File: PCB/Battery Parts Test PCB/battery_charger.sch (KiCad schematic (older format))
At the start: 43 parts, among them P5 CONN_2, P6 CONN_2, P7 CONN_2, P8 CONN_2, P9 CONN_2, Q13 MOSFET_N, Q14 MOSFET_P, Q15 MOSFET_P, T1 TRANSFO, U3 LTC4000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

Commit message: updated schematic
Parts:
- added C32: C, symbol C
- added R60: R, symbol R
- C31: value C -> 0.1uF
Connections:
- net CONV_OUT: now also C30.1
- net at P8.1 (P1), Q15.S, R50.2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: now also C31.1
- net at U3.24 (ITH), U4.2 (ITH): now also R60.2
- net at U3.25 (CC): now also C32.1
- new net: C32.2, R60.1
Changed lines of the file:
@@
-EESchema Schematic File Version 2  date 4/30/2013 1:48:29 PM
+EESchema Schematic File Version 2  date 5/7/2013 3:13:49 PM
 LIBS:power
 LIBS:device
@@
 Sheet 9 9
 Title ""
-Date "30 apr 2013"
+Date "7 may 2013"
 Rev ""
 Comp ""
@@
 Comment4 ""
 $EndDescr
-Text Label 8900 2150 0    60   ~ 0
-BATT+
+Connection ~ 9700 1350
+Wire Wire Line
+	9700 1350 10500 1350
+Wire Wire Line
+	5250 3800 5050 3800
+Wire Wire Line
+	5050 3800 5050 2650
+Wire Wire Line
+	5050 2650 5200 2650
 Connection ~ 8250 4300
 Wire Wire Line
@@
 Wire Wire Line
 	6850 4300 7350 4300
+Connection ~ 8850 5800
+Wire Wire Line
+	6150 3800 6150 3600
+Connection ~ 6150 3600
+$Comp
+L R R60
+U 1 1 518484F7
+P 5900 3800
+F 0 "R60" V 5980 3800 50  0000 C CNN
+F 1 "R" V 5900 3800 50  0000 C CNN
+	1    5900 3800
+	0    -1   -1   0
+$EndComp
+$Comp
+L C C32
+U 1 1 518484F3
+P 5450 3800
+F 0 "C32" H 5500 3900 50  0000 L CNN
+F 1 "C" H 5500 3700 50  0000 L CNN
+	1    5450 3800
+	0    -1   -1   0
+$EndComp
+Text Label 8900 2150 0    60   ~ 0
+BATT+
 Text Label 6350 850  0    60   ~ 0
 VIN
@@
 CONV_OUT
 $Comp
-L GND #PWR9
+L GND #PWR011
 U 1 1 51756554
 P 6350 4950
-F 0 "#PWR9" H 6350 4950 30  0001 C CNN
+F 0 "#PWR011" H 6350 4950 30  0001 C CNN
 F 1 "GND" H 6350 4880 30  0001 C CNN
 	1    6350 4950
@@
 $EndComp
 $Comp
-L GND #PWR11
+L GND #PWR012
 U 1 1 517562CD
 P 6500 6400
-F 0 "#PWR11" H 6500 6400 30  0001 C CNN
+F 0 "#PWR012" H 6500 6400 30  0001 C CNN
 F 1 "GND" H 6500 6330 30  0001 C CNN
 	1    6500 6400
@@
 $EndComp
 $Comp
-L GND #PWR16
+L GND #PWR013
 U 1 1 5175625C
 P 8600 6400
-F 0 "#PWR16" H 8600 6400 30  0001 C CNN
+F 0 "#PWR013" H 8600 6400 30  0001 C CNN
 F 1 "GND" H 8600 6330 30  0001 C CNN
 	1    8600 6400
@@
 $EndComp
 $Comp
-L GND #PWR12
+L GND #PWR014
 U 1 1 517560C1
 P 6650 5100
-F 0 "#PWR12" H 6650 5100 30  0001 C CNN
+F 0 "#PWR014" H 6650 5100 30  0001 C CNN
 F 1 "GND" H 6650 5030 30  0001 C CNN
 	1    6650 5100
@@
 $EndComp
 $Comp
-L GND #PWR18
+L GND #PWR015
 U 1 1 51755E2F
 P 10150 2350
-F 0 "#PWR18" H 10150 2350 30  0001 C CNN
+F 0 "#PWR015" H 10150 2350 30  0001 C CNN
 F 1 "GND" H 10150 2280 30  0001 C CNN
 	1    10150 2350
@@
 $EndComp
 $Comp
-L GND #PWR8
+L GND #PWR016
 U 1 1 51755B48
 P 3800 5250
-F 0 "#PWR8" H 3800 5250 30  0001 C CNN
+F 0 "#PWR016" H 3800 5250 30  0001 C CNN
 F 1 "GND" H 3800 5180 30  0001 C CNN
 	1    3800 5250
@@
 $EndComp
 $Comp
-L GND #PWR7
+L GND #PWR017
 U 1 1 517552C5
 P 2250 3250
-F 0 "#PWR7" H 2250 3250 30  0001 C CNN
+F 0 "#PWR017" H 2250 3250 30  0001 C CNN
 F 1 "GND" H 2250 3180 30  0001 C CNN
 	1    2250 3250
@@
 Output Voltage to System
 $Comp
-L GND #PWR17
+L GND #PWR018
 U 1 1 5169B996
 P 10150 1150
-F 0 "#PWR17" H 10150 1150 30  0001 C CNN
+F 0 "#PWR018" H 10150 1150 30  0001 C CNN
 F 1 "GND" H 10150 1080 30  0001 C CNN
 	1    10150 1150
@@
 $EndComp
 $Comp
-L GND #PWR19
+L GND #PWR019
 U 1 1 5169B959
 P 10500 1750
-F 0 "#PWR19" H 10500 1750 30  0001 C CNN
+F 0 "#PWR019" H 10500 1750 30  0001 C CNN
 F 1 "GND" H 10500 1680 30  0001 C CNN
 	1    10500 1750
@@
 P 10500 1550
 F 0 "C31" H 10550 1650 50  0000 L CNN
-F 1 "C" H 10550 1450 50  0000 L CNN
+F 1 "0.1uF" H 10550 1450 50  0000 L CNN
 	1    10500 1550
 	1    0    0    -1
@@
 $EndComp
 $Comp
-L GND #PWR15
+L GND #PWR020
 U 1 1 5169B8A2
 P 8400 5100
-F 0 "#PWR15" H 8400 5100 30  0001 C CNN
+F 0 "#PWR020" H 8400 5100 30  0001 C CNN
 F 1 "GND" H 8400 5030 30  0001 C CNN
 	1    8400 5100
@@
 $EndComp
 $Comp
-L GND #PWR13
+L GND #PWR021
 U 1 1 5169B850
 P 7400 1450
-F 0 "#PWR13" H 7400 1450 30  0001 C CNN
+F 0 "#PWR021" H 7400 1450 30  0001 C CNN
 F 1 "GND" H 7400 1380 30  0001 C CNN
 	1    7400 1450
@@
 $EndComp
 $Comp
-L GND #PWR10
+L GND #PWR022
 U 1 1 5169B80F
 P 6450 2900
-F 0 "#PWR10" H 6450 2900 30  0001 C CNN
+F 0 "#PWR022" H 6450 2900 30  0001 C CNN
 F 1 "GND" H 6450 2830 30  0001 C CNN
 	1    6450 2900
@@
 $EndComp
 $Comp
-L GND #PWR14
+L GND #PWR023
 U 1 1 5169B7FD
 P 7700 1000
-F 0 "#PWR14" H 7700 1000 30  0001 C CNN
+F 0 "#PWR023" H 7700 1000 30  0001 C CNN
 F 1 "GND" H 7700 930 30  0001 C CNN
 	1    7700 1000

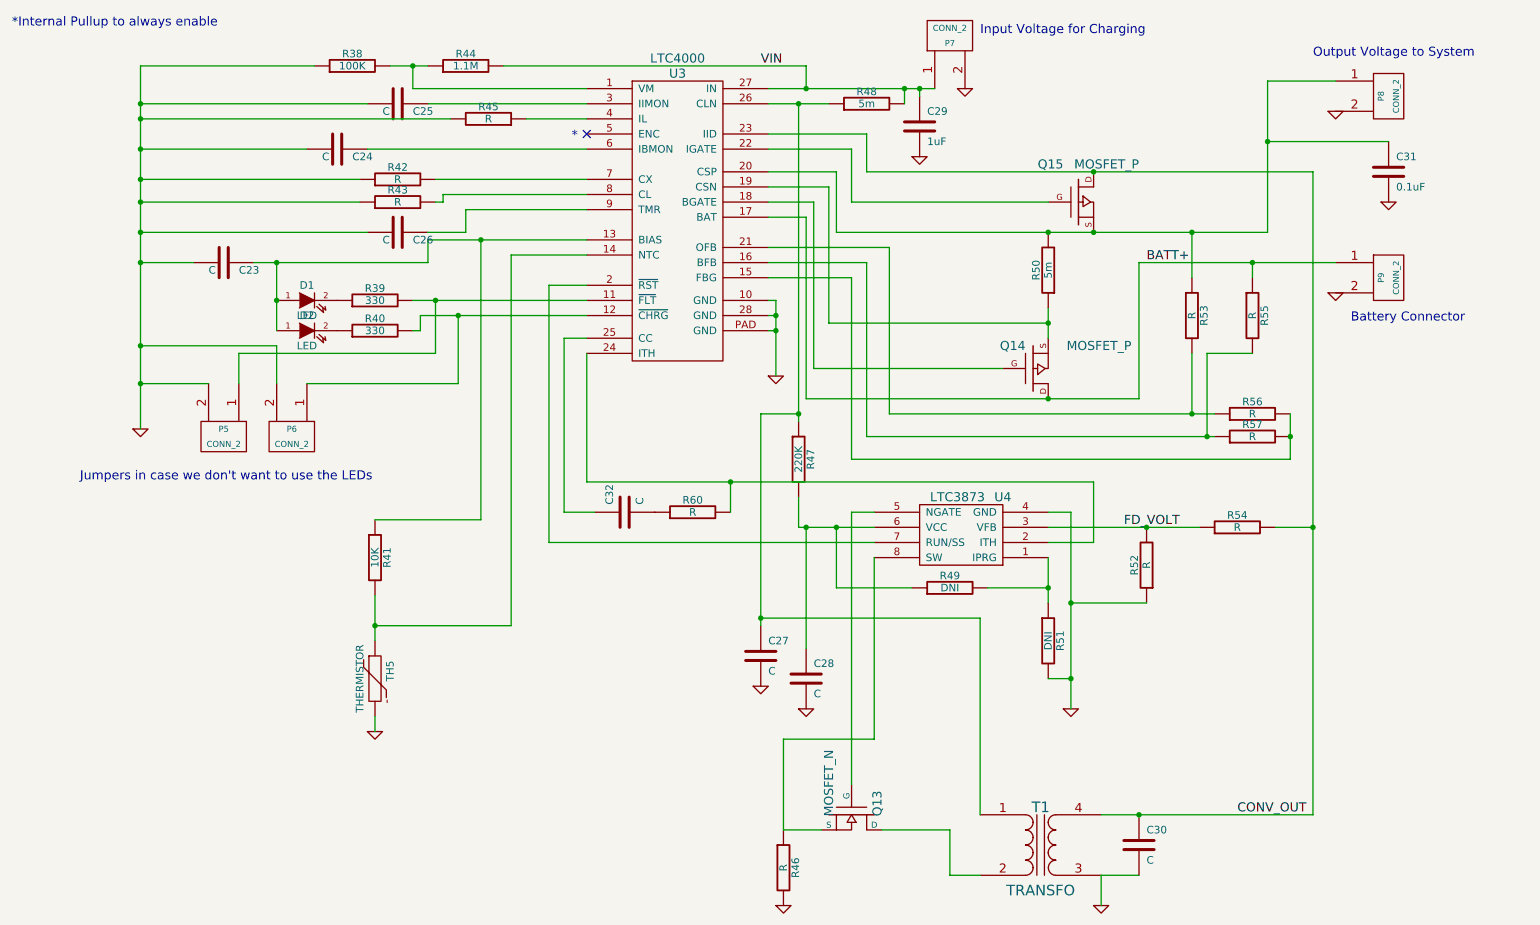
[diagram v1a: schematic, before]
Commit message: update of new pcb and power supply design
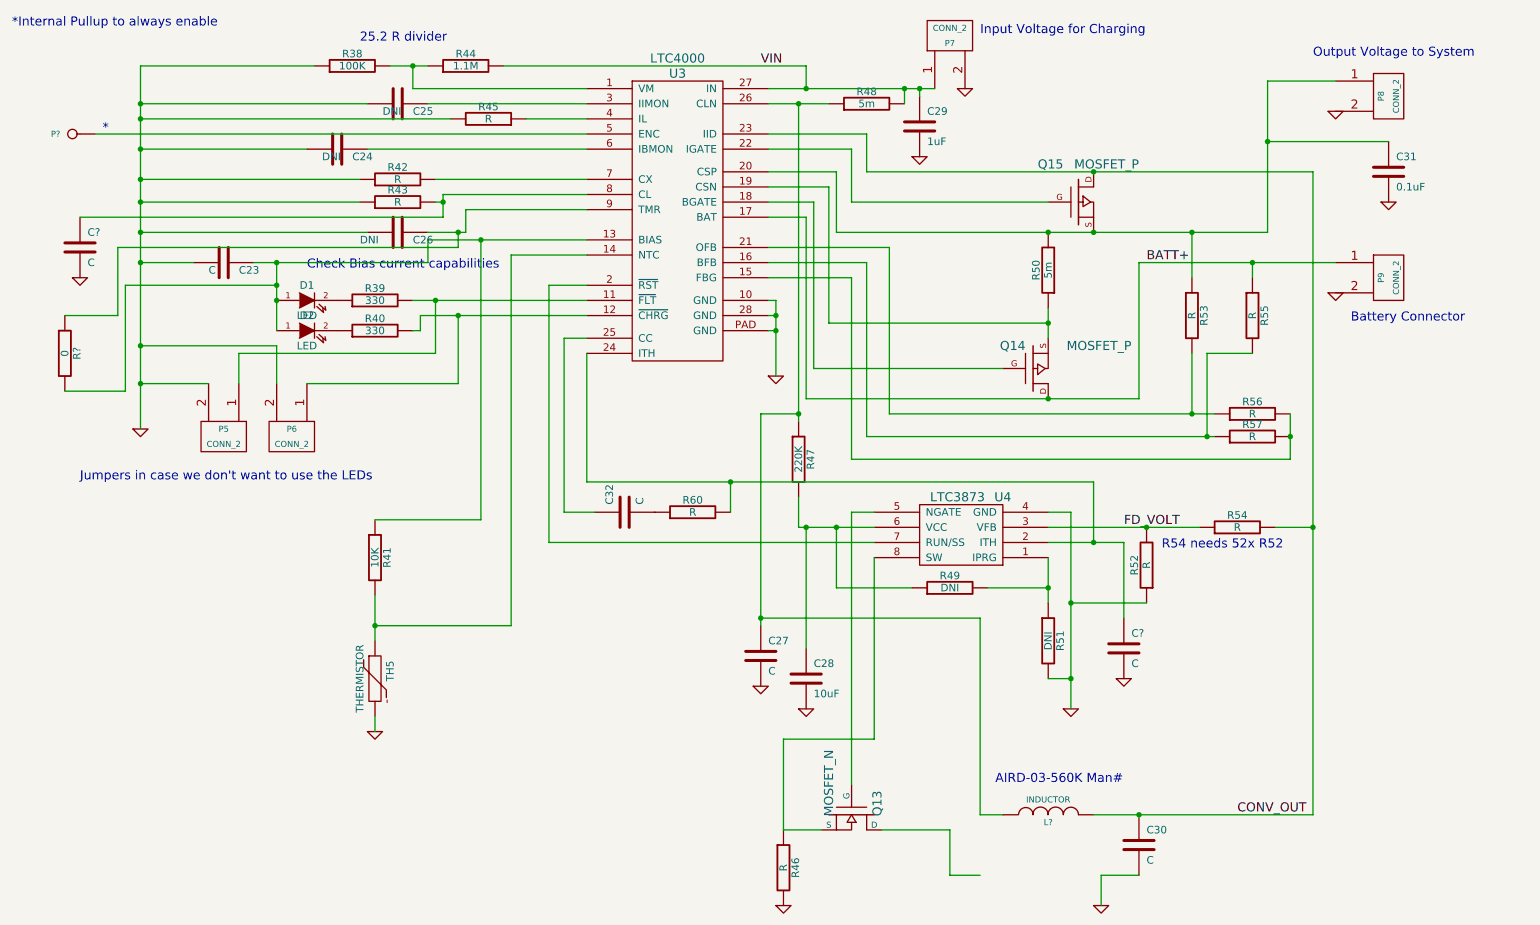
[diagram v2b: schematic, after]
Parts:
- removed T1: TRANSFO, symbol TRANSFO
- added C? (x2): C, symbol C
- added L?: INDUCTOR, symbol INDUCTOR
- added P?: CONN_1, symbol CONN_1
- added R?: 0, symbol R
- C24, C25, C26: value C -> DNI
- C28: value C -> 10uF
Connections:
- net CONV_OUT: now also L?.2
- net GND: now also C?.2, C?.2
- net at C23.1, D1.1 (A), D2.1 (A)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: now also R?.2
- net at R60.2, U3.24 (ITH), U4.2 (ITH): now also C?.1
- net at C27.1, R47.1, R48.1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: now also L?.1
- net at U3.5 (ENC): now also P?.1
- net at R43.2, U3.8 (CL): now also C?.1
- net at C26.1, U3.9 (TMR): now also R?.1
- no-connect marks 1 -> 0
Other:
- note added: "25.2 R divider"
- note added: "AIRD-03-560K Man#"
- note added: "Check Bias current capabilities"
- note added: "R54 needs 52x R52"
